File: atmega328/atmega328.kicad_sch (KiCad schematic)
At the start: 11 parts, among them SW201 default_switch, SW202 default_switch, U201 HEADER_3x2, U202 ATmega328-A, Y201 Crystal_GND2

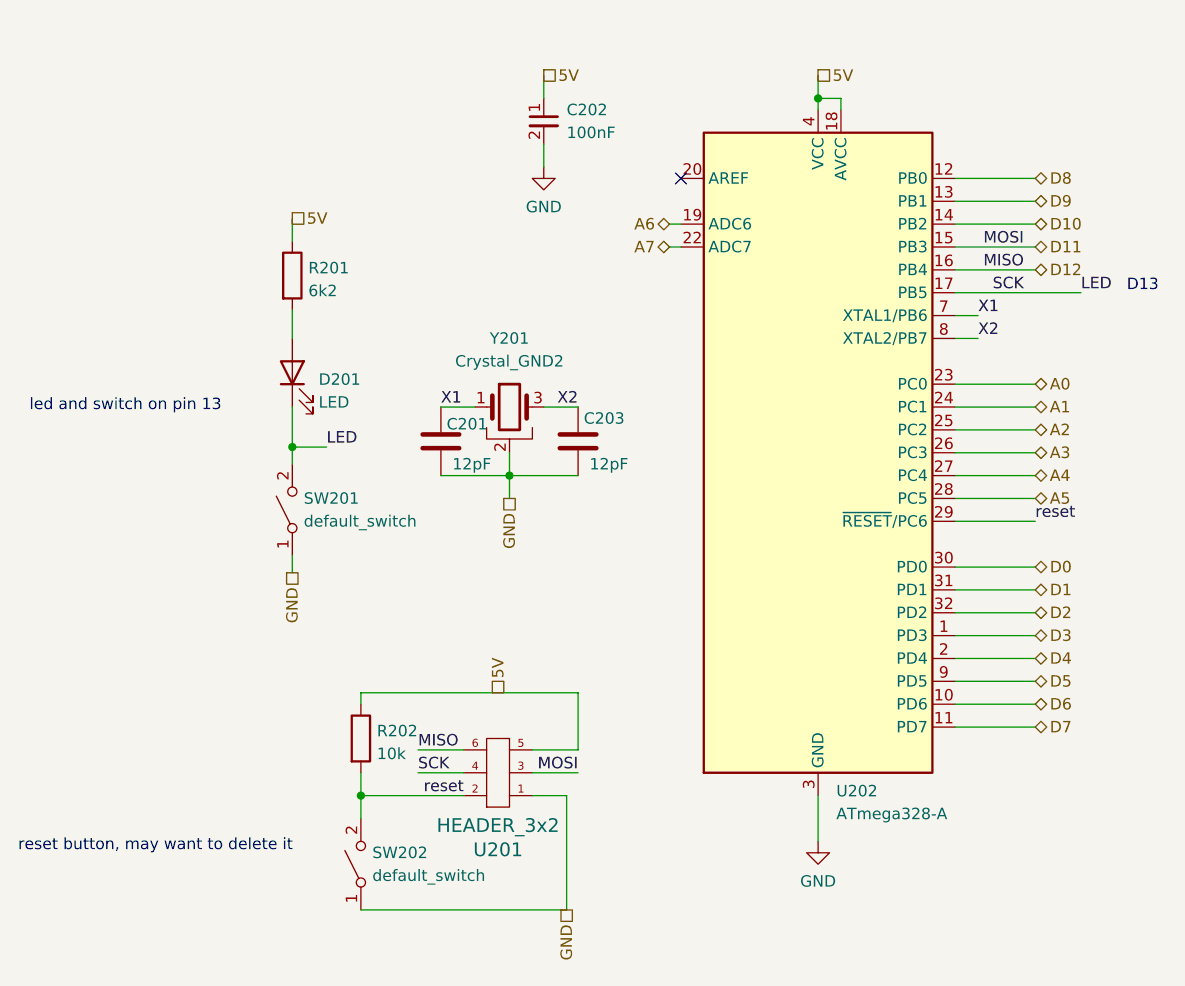
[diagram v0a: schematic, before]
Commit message: added 12V boost converter (300mA max!)
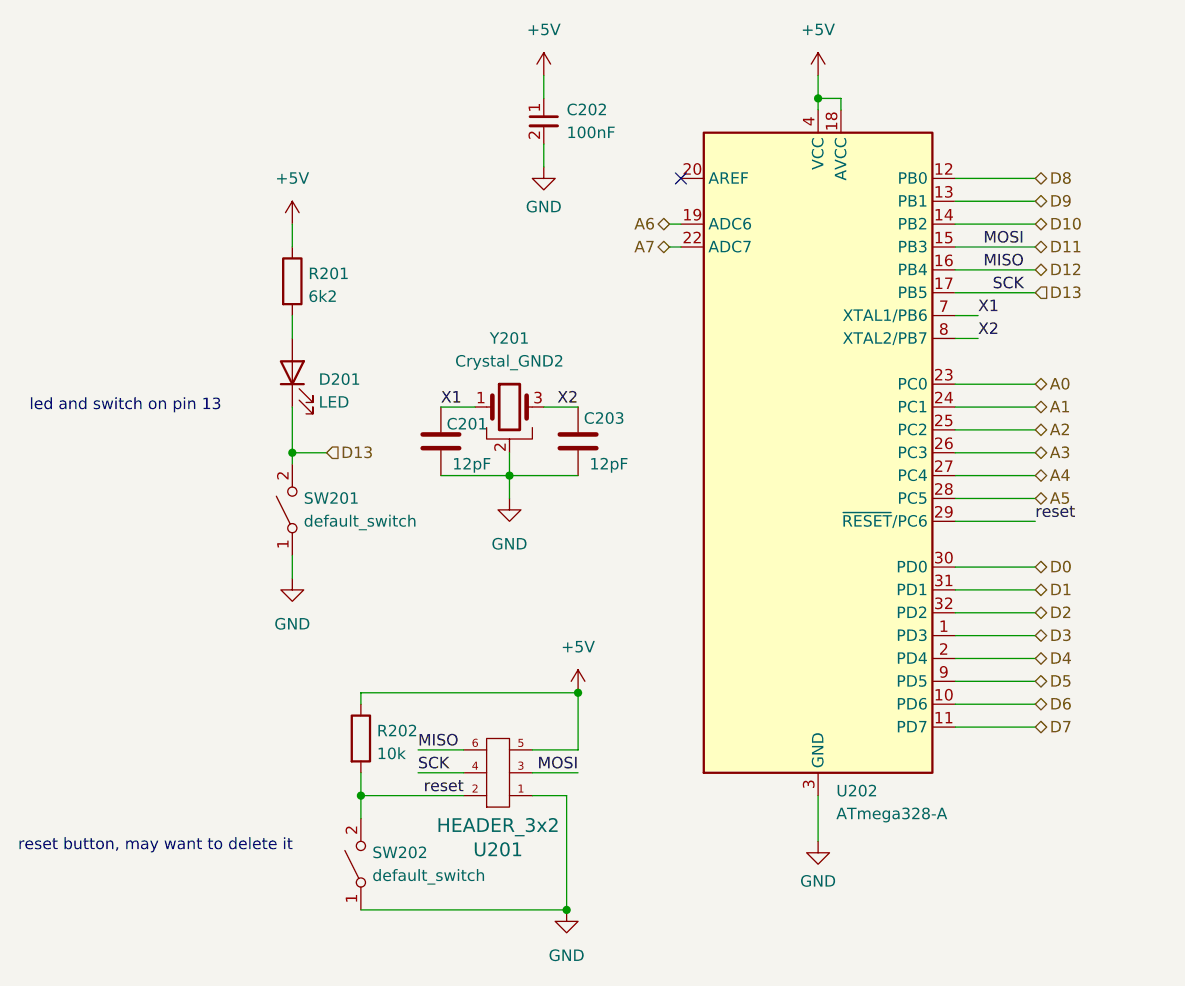
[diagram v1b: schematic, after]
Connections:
- net 5V renamed +5V
- net LED renamed D13
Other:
- note removed: "D13"
- moved on the sheet: R201
